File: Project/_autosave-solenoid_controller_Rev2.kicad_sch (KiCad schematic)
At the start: 110 parts, among them J1 Conn_01x04_Pin, J10 Conn_01x02_Socket, J11 Conn_01x02_Socket, J12 Conn_01x02_Socket, J13 Conn_01x02_Socket, J14 Conn_01x02_Socket, J15 Conn_01x02_Socket, J16 Conn_01x02_Socket, J17 Conn_01x02_Socket, J18 Conn_01x02_Socket, J19 Conn_01x02_Socket, J2 Conn_01x06_Socket, J20 Conn_01x02_Socket, J21 Conn_02x05_Odd_Even, J22 Conn_01x04_Pin, J3 Conn_01x06_Socket, J4 Conn_01x02_Socket, J5 Conn_01x02_Socket, J6 Conn_01x02_Socket, J7 Conn_01x02_Socket, J8 Conn_01x02_Socket, J9 Conn_01x02_Socket, SW1 SW_MEC_5E, U1 SSM6N7002KFU, U2 FT231XS-R, U3 THVD2442, U4 NCP1117-3.3_SOT223, U5 SSM6N7002KFU, U6 DAC60502, U7 NCV272DMR2G, U8 NCV272DMR2G, Y1 ABM8-24.000MHZ-R60-D1W-T

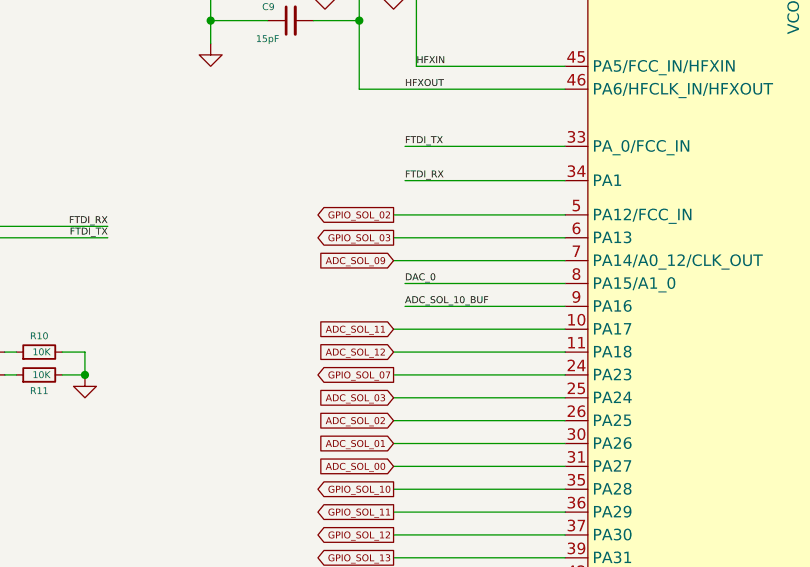
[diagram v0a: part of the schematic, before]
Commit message: finished schematic and footprint assignments
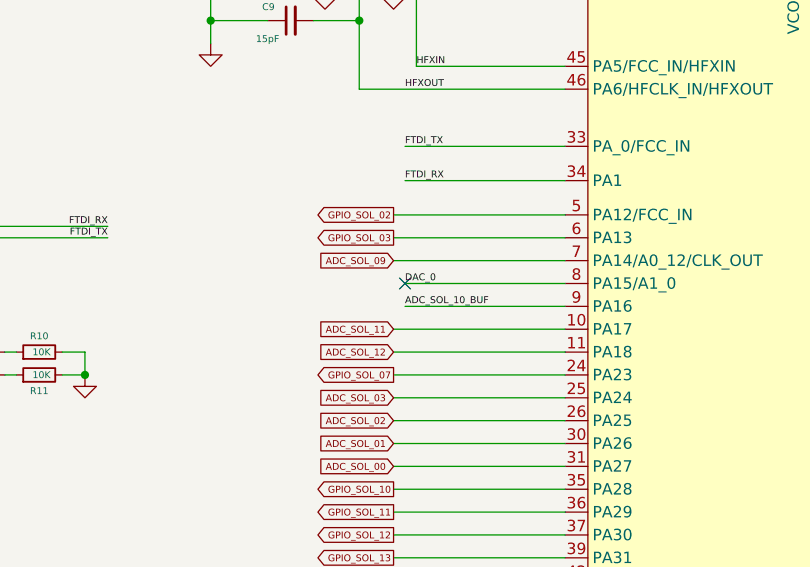
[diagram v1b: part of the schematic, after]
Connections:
- no-connect marks 28 -> 29
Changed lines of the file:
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@@
+	)
+	(no_connect
+		(at 128.27 128.27)
 	)
 	(no_connect
